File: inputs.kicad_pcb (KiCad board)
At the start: 2 copper layers, 114 x 71 mm, 46 parts, among them J1 Conn_01x15, J2 2601-3106, J3 2601-3109, J4 HTSW-217-15-T-S, U1 PC817, U10 PC817, U11 PC817, U12 PC817, U13 PC817, U14 PC817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

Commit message: Move to 2 8Pin Wagos
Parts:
- removed J1: Conn_01x15, Connector_PinHeader_2.54mm:PinHeader_1x15_P2.54mm_Vertical
- removed J2: 2601-3106, 3106:CONN_2601-3106_WAG
- removed J3: 2601-3109, 3109:CONN9_2601-3109_WAG
- added J5: 2601-3108, 3108:CONN8_2601-3108_WAG, F.Cu at (132.3, 59.3)
- added J6: 2601-3108, 3108:CONN8_2601-3108_WAG, F.Cu at (189.3, 59.3)
- moved J4 17.7 mm to (170.4, 99.0)
- moved R1 17.7 mm to (124.0, 73.4)
- moved R10 17.7 mm to (161.9, 73.4)
- moved R11 17.7 mm to (169.4, 73.4)
- moved R12 17.7 mm to (177.0, 73.4)
- moved R13 17.7 mm to (154.3, 92.5)
- moved R14 17.7 mm to (161.9, 92.5)
- moved R15 17.7 mm to (169.4, 92.5)
- moved R16 17.7 mm to (177.0, 92.5)
- moved R17 17.7 mm to (184.6, 73.4)
- moved R18 17.7 mm to (192.1, 73.4)
- moved R19 17.7 mm to (199.7, 73.4)
- moved R2 17.7 mm to (131.6, 73.4)
- moved R20 17.7 mm to (207.3, 73.4)
- moved R21 17.7 mm to (184.6, 92.5)
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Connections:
- J4 pad 15: unconnected-(J4-Pad15) -> GND
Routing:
- net GND: track 207.1 -> 248.7 mm
- net /in14: track 23.9 -> 16.8 mm
- net /in13: track 19.8 -> 14.2 mm
- net /in1: track 21.4 -> 16.5 mm
- net /in12: track 15.9 -> 12.5 mm
- net /in9: track 11.7 -> 14.8 mm
- net /in7: track 14.4 -> 17.3 mm
- net /in2: track 17.3 -> 14.5 mm
- net /in11: track 14.2 -> 11.4 mm
- net /in6: track 12.7 -> 14.9 mm
- net /in3: track 14.8 -> 12.8 mm
- net /in5: track 11.4 -> 13.2 mm
- net /in4: track 13.1 -> 11.5 mm
- net /in8: track 16.4 -> 17.5 mm
- net /in10: track 12.5 -> 13.1 mm
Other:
- board text added: "+24v"
- board text added: "Com-"

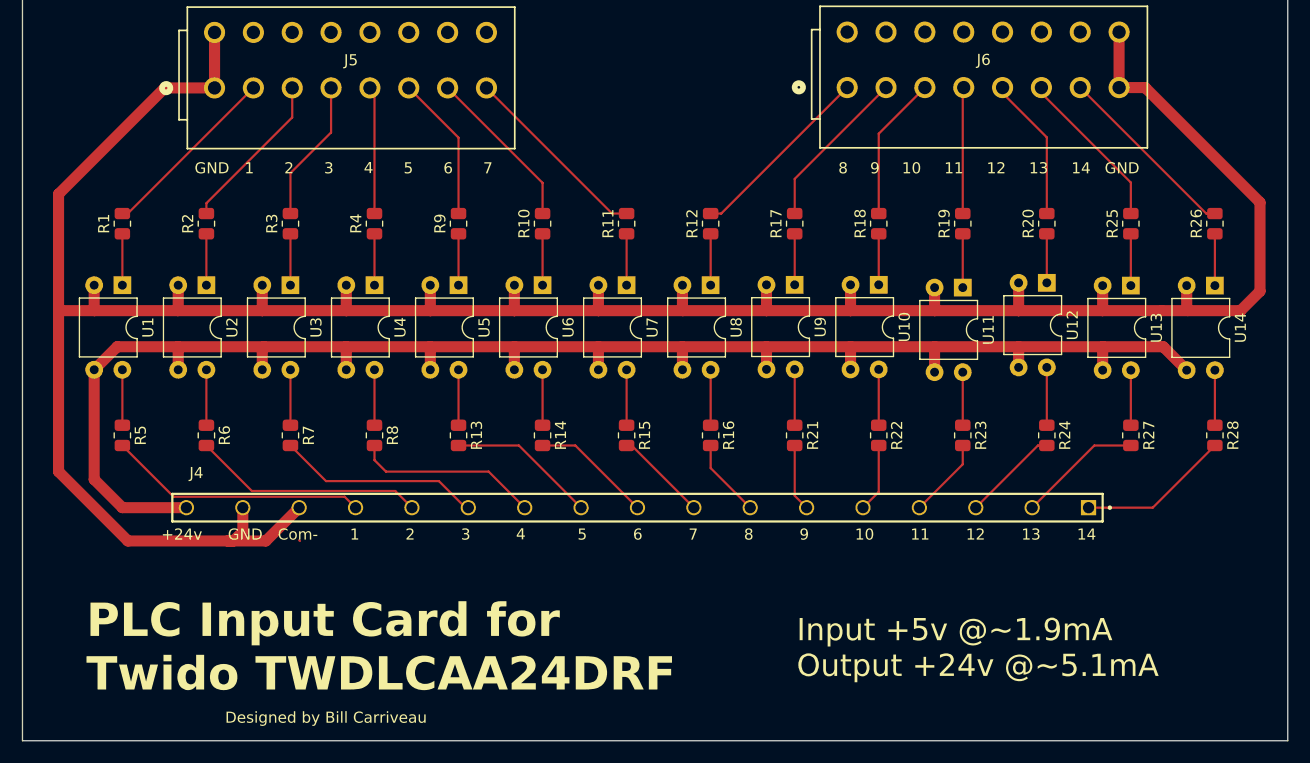
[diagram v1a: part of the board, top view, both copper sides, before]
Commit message: Add Common GND Jumpers, split 5v/24v, Add LEDS
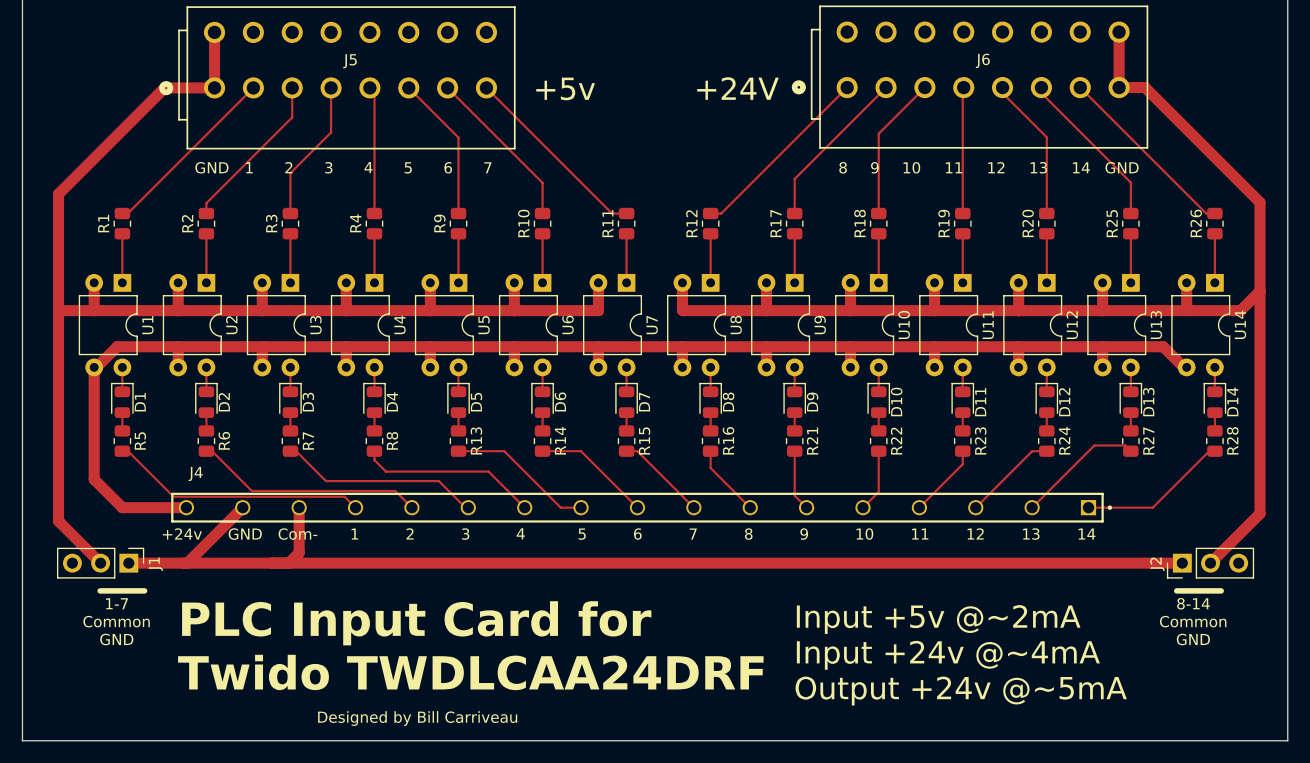
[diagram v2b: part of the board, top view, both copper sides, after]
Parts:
- added D1: LED, LED_SMD:LED_0805_2012Metric, F.Cu at (124.0, 89.5)
- added D10: LED, LED_SMD:LED_0805_2012Metric, F.Cu at (192.1, 89.5)
- added D11: LED, LED_SMD:LED_0805_2012Metric, F.Cu at (199.7, 89.5)
- added D12: LED, LED_SMD:LED_0805_2012Metric, F.Cu at (207.3, 89.5)
- added D13: LED, LED_SMD:LED_0805_2012Metric, F.Cu at (214.9, 89.5)
- added D14: LED, LED_SMD:LED_0805_2012Metric, F.Cu at (222.4, 89.5)
- added D2: LED, LED_SMD:LED_0805_2012Metric, F.Cu at (131.6, 89.5)
- added D3: LED, LED_SMD:LED_0805_2012Metric, F.Cu at (139.1, 89.5)
- added D4: LED, LED_SMD:LED_0805_2012Metric, F.Cu at (146.7, 89.5)
- added D5: LED, LED_SMD:LED_0805_2012Metric, F.Cu at (154.3, 89.5)
- added D6: LED, LED_SMD:LED_0805_2012Metric, F.Cu at (161.9, 89.5)
- added D7: LED, LED_SMD:LED_0805_2012Metric, F.Cu at (169.4, 89.5)
- added D8: LED, LED_SMD:LED_0805_2012Metric, F.Cu at (177.0, 89.5)
- added D9: LED, LED_SMD:LED_0805_2012Metric, F.Cu at (184.6, 89.5)
- added J1: Conn_01x03, Connector_PinHeader_2.54mm:PinHeader_1x03_P2.54mm_Vertical, F.Cu at (124.6, 104.0)
- added J2: Conn_01x03, Connector_PinHeader_2.54mm:PinHeader_1x03_P2.54mm_Vertical, F.Cu at (219.5, 104.0)
- R12, R17, R18, R19, R20, R25, R26: value 2k -> 5.6k
- R13, R14, R15, R16, R21, R22, R23, R24, R27, R28, R5, R6, R7, R8: value 4.7k -> 4.3k
- moved R16 0.51 mm to (177.0, 93.0)
- moved R13 0.51 mm to (154.3, 93.0)
- moved R14 0.51 mm to (161.9, 93.0)
- moved R15 0.51 mm to (169.4, 93.0)
- moved R21 0.51 mm to (184.6, 93.0)
- moved R22 0.51 mm to (192.1, 93.0)
- moved R23 0.51 mm to (199.7, 93.0)
- moved R24 0.51 mm to (207.3, 93.0)
- moved R27 0.51 mm to (214.9, 93.0)
- moved R28 0.51 mm to (222.4, 93.0)
- moved R5 0.51 mm to (124.0, 93.0)
- moved R6 0.51 mm to (131.6, 93.0)
- moved R7 0.51 mm to (139.1, 93.0)
- moved R8 0.51 mm to (146.7, 93.0)
- moved U11 0.43 mm to (199.7, 78.7)
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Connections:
- R13 pad 1: Net-(R13-Pad1) -> Net-(D5-A)
- R14 pad 1: Net-(R14-Pad1) -> Net-(D6-A)
- R15 pad 1: Net-(R15-Pad1) -> Net-(D7-A)
- R16 pad 1: Net-(R16-Pad1) -> Net-(D8-A)
- R21 pad 1: Net-(R21-Pad1) -> Net-(D9-A)
- R22 pad 1: Net-(R22-Pad1) -> Net-(D10-A)
- R23 pad 1: Net-(R23-Pad1) -> Net-(D11-A)
- R24 pad 1: Net-(R24-Pad1) -> Net-(D12-A)
- R27 pad 1: Net-(R27-Pad1) -> Net-(D13-A)
- R28 pad 1: Net-(R28-Pad1) -> Net-(D14-A)
- R5 pad 1: Net-(R5-Pad1) -> Net-(D1-A)
- R6 pad 1: Net-(R6-Pad1) -> Net-(D2-A)
- R7 pad 1: Net-(R7-Pad1) -> Net-(D3-A)
- R8 pad 1: Net-(R8-Pad1) -> Net-(D4-A)
- U1 pad 4: Net-(R5-Pad1) -> Net-(D1-K)
- U10 pad 4: Net-(R22-Pad1) -> Net-(D10-K)
- U11 pad 4: Net-(R23-Pad1) -> Net-(D11-K)
- U12 pad 4: Net-(R24-Pad1) -> Net-(D12-K)
- U13 pad 4: Net-(R27-Pad1) -> Net-(D13-K)
- U14 pad 4: Net-(R28-Pad1) -> Net-(D14-K)
- U2 pad 4: Net-(R6-Pad1) -> Net-(D2-K)
- U3 pad 4: Net-(R7-Pad1) -> Net-(D3-K)
- U4 pad 4: Net-(R8-Pad1) -> Net-(D4-K)
- U5 pad 4: Net-(R13-Pad1) -> Net-(D5-K)
- U6 pad 4: Net-(R14-Pad1) -> Net-(D6-K)
- U7 pad 4: Net-(R15-Pad1) -> Net-(D7-K)
- U8 pad 4: Net-(R16-Pad1) -> Net-(D8-K)
- U9 pad 4: Net-(R21-Pad1) -> Net-(D9-K)
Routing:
- net GND: track 248.7 -> 357.0 mm
- net Net-(R24-Pad1): track 5.21 -> 0.00 mm
- net Net-(R22-Pad1): track 5.03 -> 0.00 mm
- net Net-(R21-Pad1): track 5.03 -> 0.00 mm
- net Net-(R8-Pad1): track 5.00 -> 0.00 mm
- net Net-(R7-Pad1): track 5.00 -> 0.00 mm
- net Net-(R6-Pad1): track 5.00 -> 0.00 mm
- net Net-(R5-Pad1): track 5.00 -> 0.00 mm
- net Net-(R16-Pad1): track 5.00 -> 0.00 mm
- net Net-(R15-Pad1): track 5.00 -> 0.00 mm
- net Net-(R14-Pad1): track 5.00 -> 0.00 mm
- net Net-(R13-Pad1): track 5.00 -> 0.00 mm
- net Net-(R28-Pad1): track 4.96 -> 0.00 mm
- net Net-(R27-Pad1): track 4.96 -> 0.00 mm
- net Net-(R23-Pad1): track 4.78 -> 0.00 mm
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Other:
- board text added: "+24V"
- board text added: "+5v"
- board text added: "1-7 Common GND"
- board text added: "8-14 Common GND"
- board text added: "Input +5v @~2mA Input +24v @~4mA Output +24v @~5mA"
- board text removed: "Input +5v @~1.9mA Output +24v @~5.1mA"

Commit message: update Silkscreen, update values
First board ordered
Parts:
- moved J6 1.30 mm to (188.0, 59.3)
- moved U1 1.00 mm to (124.0, 77.7)
- moved U10 1.00 mm to (192.1, 77.7)
- moved U11 1.00 mm to (199.7, 77.7)
- moved U12 1.00 mm to (207.3, 77.7)
- moved U13 1.00 mm to (214.9, 77.7)
- moved U14 1.00 mm to (222.4, 77.7)
- moved U2 1.00 mm to (131.6, 77.7)
- moved U3 1.00 mm to (139.1, 77.7)
- moved U4 1.00 mm to (146.7, 77.7)
- moved U5 1.00 mm to (154.3, 77.7)
- moved U6 1.00 mm to (161.9, 77.7)
- moved U7 1.00 mm to (169.4, 77.7)
- moved U8 1.00 mm to (177.0, 77.7)
- moved U9 1.00 mm to (184.6, 77.7)
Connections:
- J5 pad 11: unconnected-(J5-6_1-Pad11) -> /in5
- J5 pad 13: unconnected-(J5-7_1-Pad13) -> /in6
- J5 pad 15: unconnected-(J5-8_1-Pad15) -> /in7
- J5 pad 3: GND -> /in1
- J5 pad 5: unconnected-(J5-3_1-Pad5) -> /in2
- J5 pad 7: unconnected-(J5-4_1-Pad7) -> /in3
- J5 pad 9: unconnected-(J5-5_1-Pad9) -> /in4
- J6 pad 1: unconnected-(J6-1_1-Pad1) -> /in8
- J6 pad 11: unconnected-(J6-6_1-Pad11) -> /in13
- J6 pad 13: unconnected-(J6-7_1-Pad13) -> /in14
- J6 pad 3: unconnected-(J6-2_1-Pad3) -> /in9
- J6 pad 5: unconnected-(J6-3_1-Pad5) -> /in10
- J6 pad 7: unconnected-(J6-4_1-Pad7) -> /in11
- J6 pad 9: unconnected-(J6-5_1-Pad9) -> /in12
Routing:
- net /in14: track 16.8 -> 23.1 mm
- net /in12: track 12.5 -> 18.5 mm
- net /in13: track 14.2 -> 20.2 mm
- net /in11: track 11.4 -> 16.9 mm
- net /in3: track 12.8 -> 17.8 mm
- net /in7: track 17.3 -> 22.3 mm
- net /in6: track 14.9 -> 19.9 mm
- net /in5: track 13.2 -> 18.2 mm
- net /in1: track 16.5 -> 21.5 mm
- net /in4: track 11.5 -> 16.5 mm
- net /in2: track 14.5 -> 19.5 mm
- net /in9: track 14.8 -> 19.2 mm
- net /in10: track 13.1 -> 17.5 mm
- net /in8: track 17.5 -> 21.4 mm
- net GND: track 357.0 -> 358.5 mm
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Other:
- board text removed: "+24V"
